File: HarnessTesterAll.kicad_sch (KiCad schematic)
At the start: 77 parts, among them J1 I/O B, J2 I/O A, J3 Power, J4 SWD, J5 Micro_SD_Card, J7 Boot, SW1 SW_MEC_5G, SW2 RoterySwitch, U1 STM32F103RETx, U2 5v regulator, U3 3.3v Regulator, U4 MAX232, U5 TXB0108, U6 TXB0108

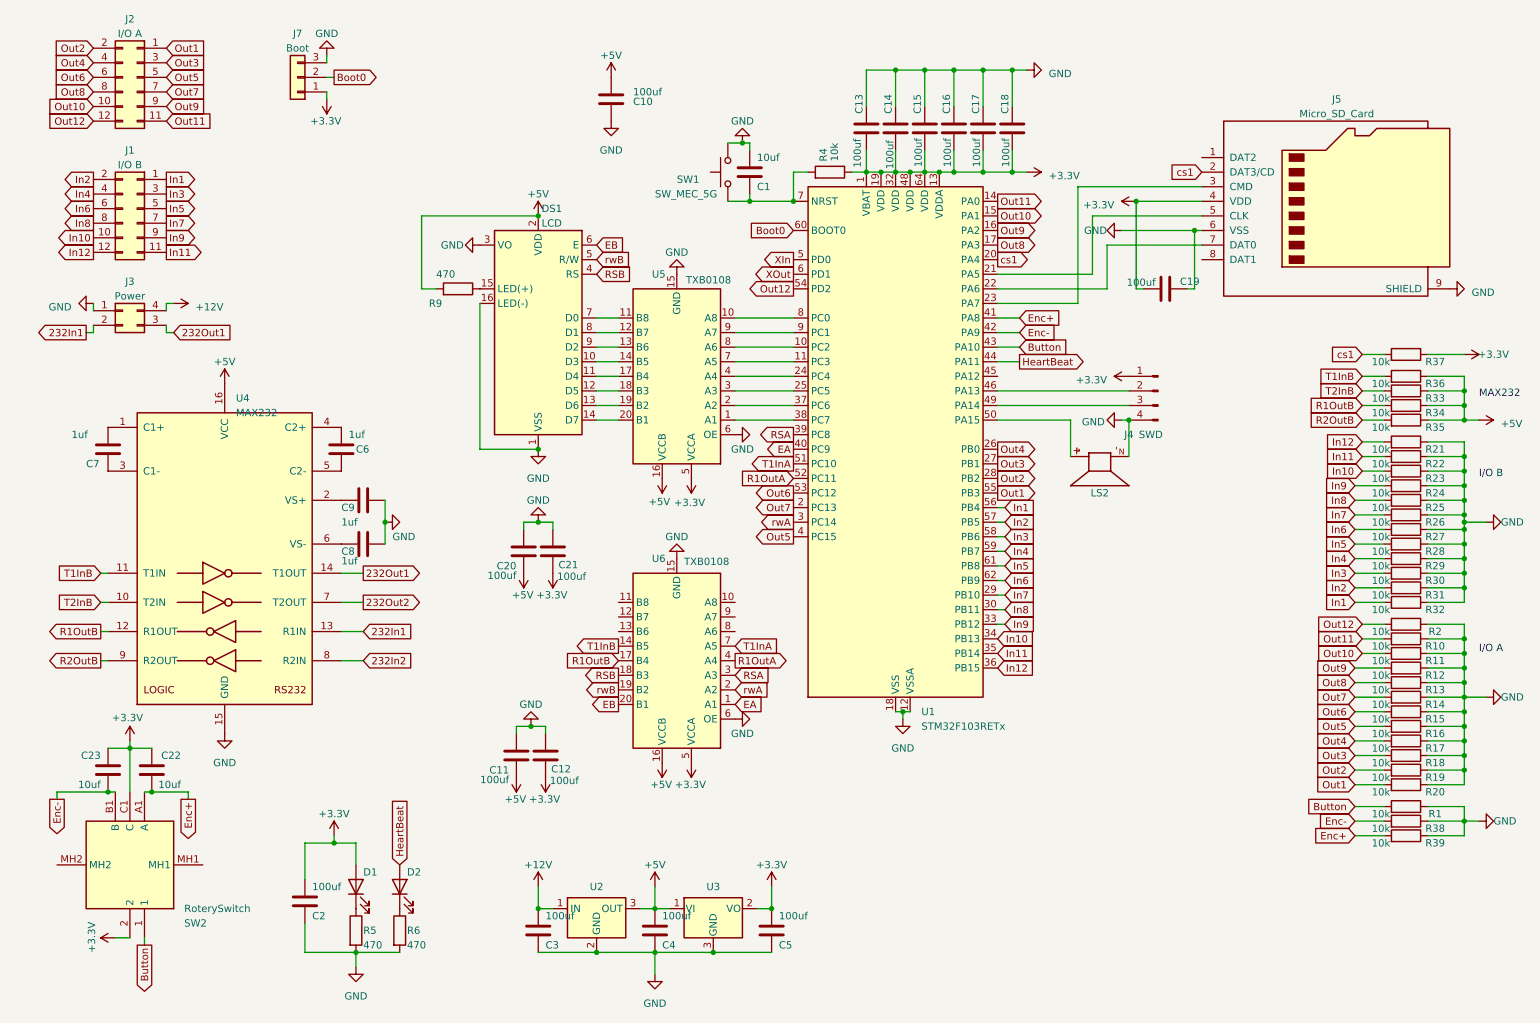
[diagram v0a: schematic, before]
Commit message: Started from scratch, Finished new schematic
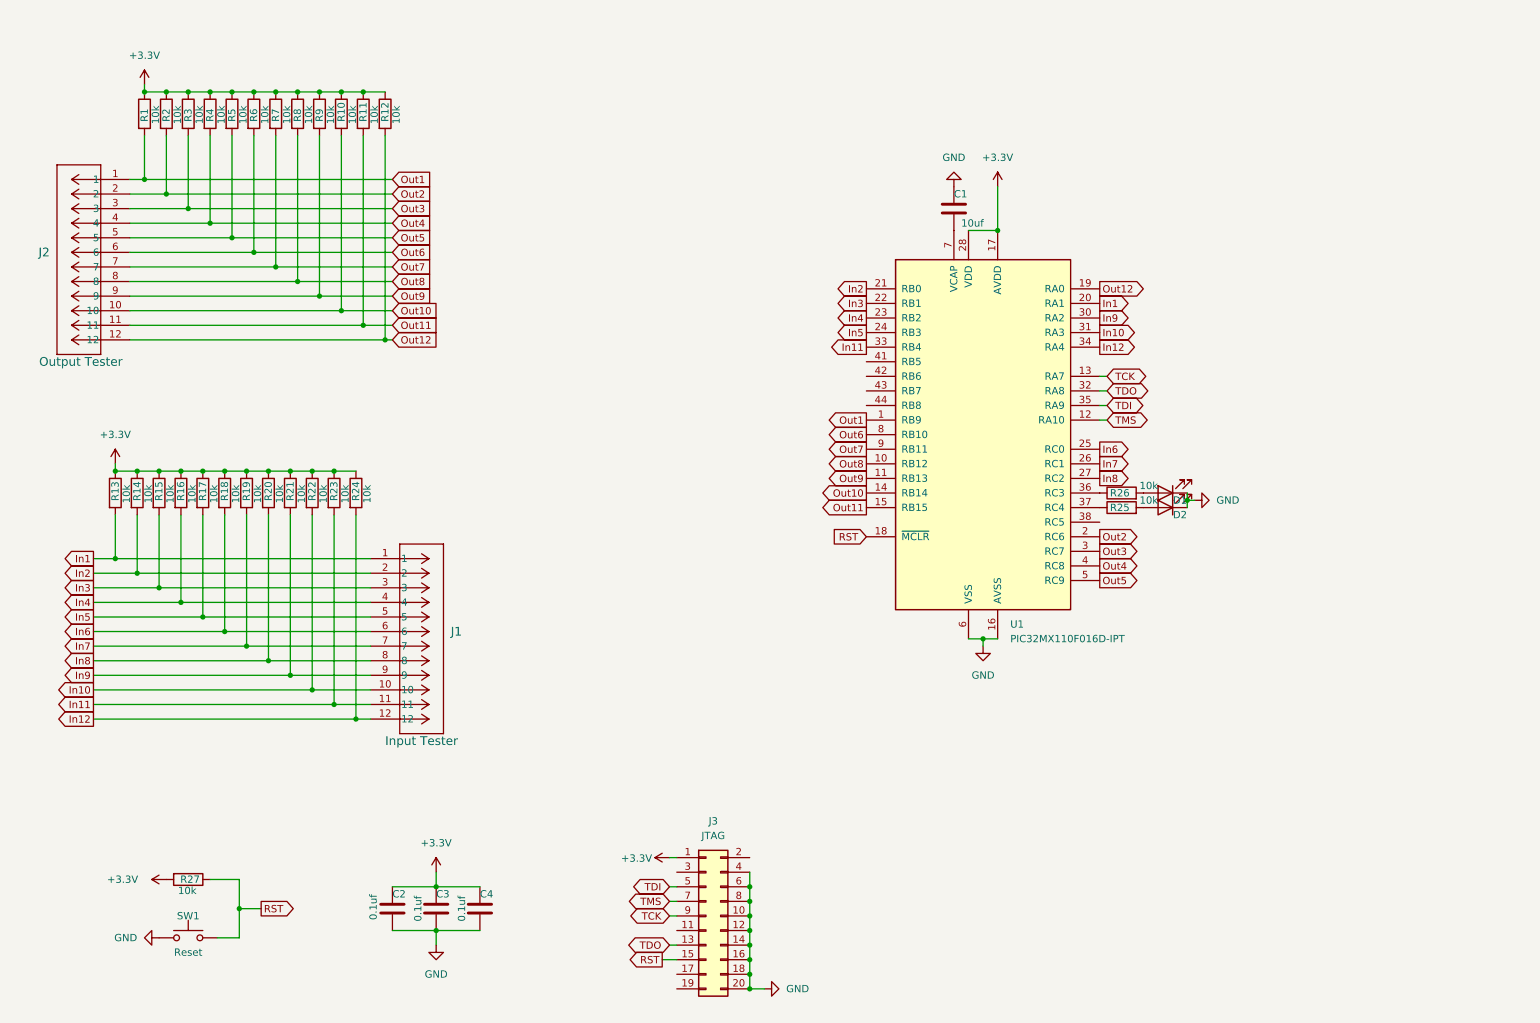
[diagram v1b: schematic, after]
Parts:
- removed C10, C11, C12, C13, C14, C15, C16, C17, C18, C19, C20, C21, C5: 100uf, Resistor_SMD:R_0603_1608Metric, symbol Device:C
- removed C22, C23: 10uf, Resistor_SMD:R_0603_1608Metric, symbol Device:C
- removed C6, C7, C8, C9: 1uf, Resistor_SMD:R_0603_1608Metric, symbol Device:C
- removed DS1: LCD, Display:WC1602A, symbol Display_Character:WC1602A
- removed J1: I/O B, Connector_Molex:Molex_Mini-Fit_Jr_5569-12A2_2x06_P4.20mm_Horizontal, symbol Connector_Generic:Conn_02x06_Odd_Even
- removed J2: I/O A, Connector_Molex:Molex_Mini-Fit_Jr_5569-12A2_2x06_P4.20mm_Horizontal, symbol Connector_Generic:Conn_02x06_Odd_Even
- removed J3: Power, Connector_Molex:Molex_Mini-Fit_Jr_5569-04A2_2x02_P4.20mm_Horizontal, symbol Connector_Generic:Conn_02x02_Counter_Clockwise
- removed J4: SWD, Connector_PinHeader_2.00mm:PinHeader_1x04_P2.00mm_Vertical, symbol Connector:Conn_01x04_Pin
- removed J5: Micro_SD_Card, DM3D:DM3DSF, symbol Connector:Micro_SD_Card
- removed J7: Boot, Connector_PinHeader_1.00mm:PinHeader_1x03_P1.00mm_Vertical, symbol Connector_Generic:Conn_01x03
- removed LS2: CMI-9605IC-0380T, CUI_CMI-9605IC-0380T, symbol CMI-9605IC-0380T:CMI-9605IC-0380T
- removed R28, R29, R30, R31, R32, R33, R34, R35, R36, R37, R38, R39: 10k, Resistor_SMD:R_0603_1608Metric, symbol Device:R
- removed SW1: SW_MEC_5G, Button_Switch_SMD:SW_MEC_5GSH9, symbol Switch:SW_MEC_5G
- removed SW2: RoterySwitch, PEC11R4220FS0024, symbol PEC11R-4220F-S0024:PEC11R-4220F-S0024
- removed U1: STM32F103RETx, Package_QFP:LQFP-64_10x10mm_P0.5mm, symbol MCU_ST_STM32F1:STM32F103RETx
- removed U2: 5v regulator, TLE42744DV50ATMA1:DPAK229P994X241-3N, symbol Converter_DCDC:OKI-78SR-5_1.5-W36-C
- removed U3: 3.3v Regulator, Package_TO_SOT_SMD:SOT-23, symbol Regulator_Linear:AP7384-33SA
- removed U4: MAX232, Max232:SOIC127P1032X265-16N, symbol Interface_UART:MAX232
- removed U5, U6: TXB0108, TXB0108PWR:SOP65P640X120-20N, symbol Logic_LevelTranslator:TXB0108DQSR
- added J1: Input Tester, Molex_2x6:CON_874271202, symbol 2024-02-18_05-42-55:874271202
- added J2: Output Tester, Molex_2x6:CON_874271202, symbol 2024-02-18_05-42-55:874271202
- added J3: JTAG, Connector_PinHeader_1.27mm:PinHeader_2x10_P1.27mm_Vertical, symbol Connector_Generic:Conn_02x10_Odd_Even
- added R3, R7, R8: 10k, Resistor_SMD:R_0603_1608Metric, symbol Device:R
- added SW1: Reset, symbol Switch:SW_Push
- added U1: PIC32MX110F016D-IPT, Package_QFP:TQFP-44_10x10mm_P0.8mm, symbol MCU_Microchip_PIC32:PIC32MX110F016D-IPT
- C1: footprint Resistor_SMD:R_0603_1608Metric -> Capacitor_SMD:C_0603_1608Metric
- C2, C3, C4: value 100uf -> 0.1uf; footprint Resistor_SMD:R_0603_1608Metric -> Capacitor_SMD:C_0603_1608Metric
- D1, D2: footprint LED_SMD:LED_0201_0603Metric -> LED_SMD:LED_0603_1608Metric
- R5, R6, R9: value 470 -> 10k
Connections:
- net +12V is gone; now on net +3.3V: C3.1
- net Button is gone; now on net Out1: R1.2
- net +3.3V: now also C4.1, R1.1, R10.1, R11.1, R12.1, R13.1, R14.1, R15.1, R16.1, R17.1, R18.1, R19.1, R2.1, R20.1, R21.1, R22.1, R23.1, R24.1, R27.2, R5.1, R6.1, R9.1, J3.1 (Pin_1), R3.1, R7.1, R8.1, U1.17 (AVDD), U1.28 (VDD), U1.40 (VDD); no longer D1.2 (A)
- net GND: now also D1.1 (K), D2.1 (K), J3.10 (Pin_10), J3.12 (Pin_12), J3.14 (Pin_14), J3.16 (Pin_16), J3.18 (Pin_18), J3.20 (Pin_20), J3.4 (Pin_4), J3.6 (Pin_6), J3.8 (Pin_8), SW1.1, U1.16 (AVSS), U1.29 (VSS), U1.39 (VSS), U1.6 (VSS); no longer R1.1, R10.1, R11.1, R12.1, R13.1, R14.1, R15.1, R16.1, R17.1, R18.1, R19.1, R2.1, R20.1, R21.1, R22.1, R23.1, R24.1, R25.1, R26.1, R27.1, R5.2, R6.2
- net In1: now also R13.2, J1.1, U1.20 (RA1)
- net In10: now also R22.2, J1.10, U1.31 (RA3); no longer R23.2
- net In11: now also R23.2, J1.11, U1.33 (RB4); no longer R22.2
- net In12: now also R24.2, J1.12, U1.34 (RA4); no longer R21.2
- net In2: now also R14.2, J1.2, U1.21 (RB0)
- net In3: now also R15.2, J1.3, U1.22 (RB1)
- net In4: now also R16.2, J1.4, U1.23 (RB2)
- net In5: now also R17.2, J1.5, U1.24 (RB3)
- net In6: now also R18.2, J1.6, U1.25 (RC0); no longer R27.2
- net In7: now also R19.2, J1.7, U1.26 (RC1); no longer R26.2
- net In8: now also R20.2, J1.8, U1.27 (RC2); no longer R25.2
- net In9: now also R21.2, J1.9, U1.30 (RA2); no longer R24.2
- net Out1: now also J2.1, U1.1 (RB9); no longer R20.2
- net Out10: now also R10.2, J2.10, U1.14 (RB14); no longer R11.2
- net Out11: now also R11.2, J2.11, U1.15 (RB15); no longer R10.2
- net Out12: now also R12.2, J2.12, U1.19 (RA0); no longer R2.2
- net Out2: now also R2.2, J2.2, U1.2 (RC6); no longer R19.2
- net Out3: now also J2.3, R3.2, U1.3 (RC7); no longer R18.2
- net Out4: now also R4.2, J2.4, U1.4 (RC8); no longer R17.2
- net Out5: now also R5.2, J2.5, U1.5 (RC9); no longer R16.2
- net Out6: now also R6.2, J2.6, U1.8 (RB10); no longer R15.2
- net Out7: now also J2.7, R7.2, U1.9 (RB11); no longer R14.2
- net Out8: now also J2.8, R8.2, U1.10 (RB12); no longer R13.2
- net Out9: now also R9.2, J2.9, U1.11 (RB13); no longer R12.2
- net at C1.2: now also U1.7 (VCAP); no longer R4.2
- removed net +5V: C4.1, R9.2
- net HeartBeat: no longer names the net of D2.2 (A)
- net HeartBeat: now also R25.2
- new net: D1.2 (A), R26.2
- new net: R26.1, U1.36 (RC3)
- new net: R25.1, U1.37 (RC4)
- new net RST: J3.15 (Pin_15), R27.1, SW1.2, U1.18 (~{MCLR})
- new net TCK: J3.9 (Pin_9), U1.13 (RA7)
- new net TDI : J3.5 (Pin_5), U1.35 (RA9)
- new net TDO: J3.13 (Pin_13), U1.32 (RA8)
- new net TMS: J3.7 (Pin_7), U1.12 (RA10)
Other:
- note removed: "I/O A"
- note removed: "I/O B"
- note removed: "MAX232"

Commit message: Made a board laylout
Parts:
- SW1: footprint (none) -> Button_Switch_SMD:SW_MEC_5GSH9
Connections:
- net In1: now also U1.34 (RA4); no longer U1.20 (RA1)
- net In10: now also U1.22 (RB1); no longer U1.31 (RA3)
- net In11: now also U1.21 (RB0); no longer U1.33 (RB4)
- net In12: now also U1.20 (RA1); no longer U1.34 (RA4)
- net In2: now also U1.33 (RB4); no longer U1.21 (RB0)
- net In3: now also U1.31 (RA3); no longer U1.22 (RB1)
- net In4: now also U1.30 (RA2); no longer U1.23 (RB2)
- net In5: now also U1.27 (RC2); no longer U1.24 (RB3)
- net In6: now also U1.26 (RC1); no longer U1.25 (RC0)
- net In7: now also U1.25 (RC0); no longer U1.26 (RC1)
- net In8: now also U1.24 (RB3); no longer U1.27 (RC2)
- net In9: now also U1.23 (RB2); no longer U1.30 (RA2)
- net Out1: now also U1.19 (RA0); no longer U1.1 (RB9)
- net Out10: now also U1.3 (RC7); no longer U1.14 (RB14)
- net Out11: now also U1.2 (RC6); no longer U1.15 (RB15)
- net Out12: now also U1.1 (RB9); no longer U1.19 (RA0)
- net Out2: now also U1.15 (RB15); no longer U1.2 (RC6)
- net Out3: now also U1.14 (RB14); no longer U1.3 (RC7)
- net Out4: now also U1.11 (RB13); no longer U1.4 (RC8)
- net Out5: now also U1.10 (RB12); no longer U1.5 (RC9)
- net Out6: now also U1.9 (RB11); no longer U1.8 (RB10)
- net Out7: now also U1.8 (RB10); no longer U1.9 (RB11)
- net Out8: now also U1.5 (RC9); no longer U1.10 (RB12)
- net Out9: now also U1.4 (RC8); no longer U1.11 (RB13)
